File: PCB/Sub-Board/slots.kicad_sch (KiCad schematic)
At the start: 119 parts, among them J10 Address, J11 Type, J12 Address, J13 Type, J14 Address, J15 Type, J16 Address, J17 Type, J18 Power/I2C, J19 GPIO, J2 Power/I2C, J20 Power/I2C, J21 GPIO, J22 Power/I2C, J23 GPIO, J24 Power/I2C, J25 GPIO, J26 Address, J27 Type, J28 Address, J29 Type, J3 GPIO, J30 Address, J31 Type, J32 Address, J33 Type, J4 Power/I2C, J5 GPIO, J6 Power/I2C, J7 GPIO, J8 Power/I2C, J9 GPIO

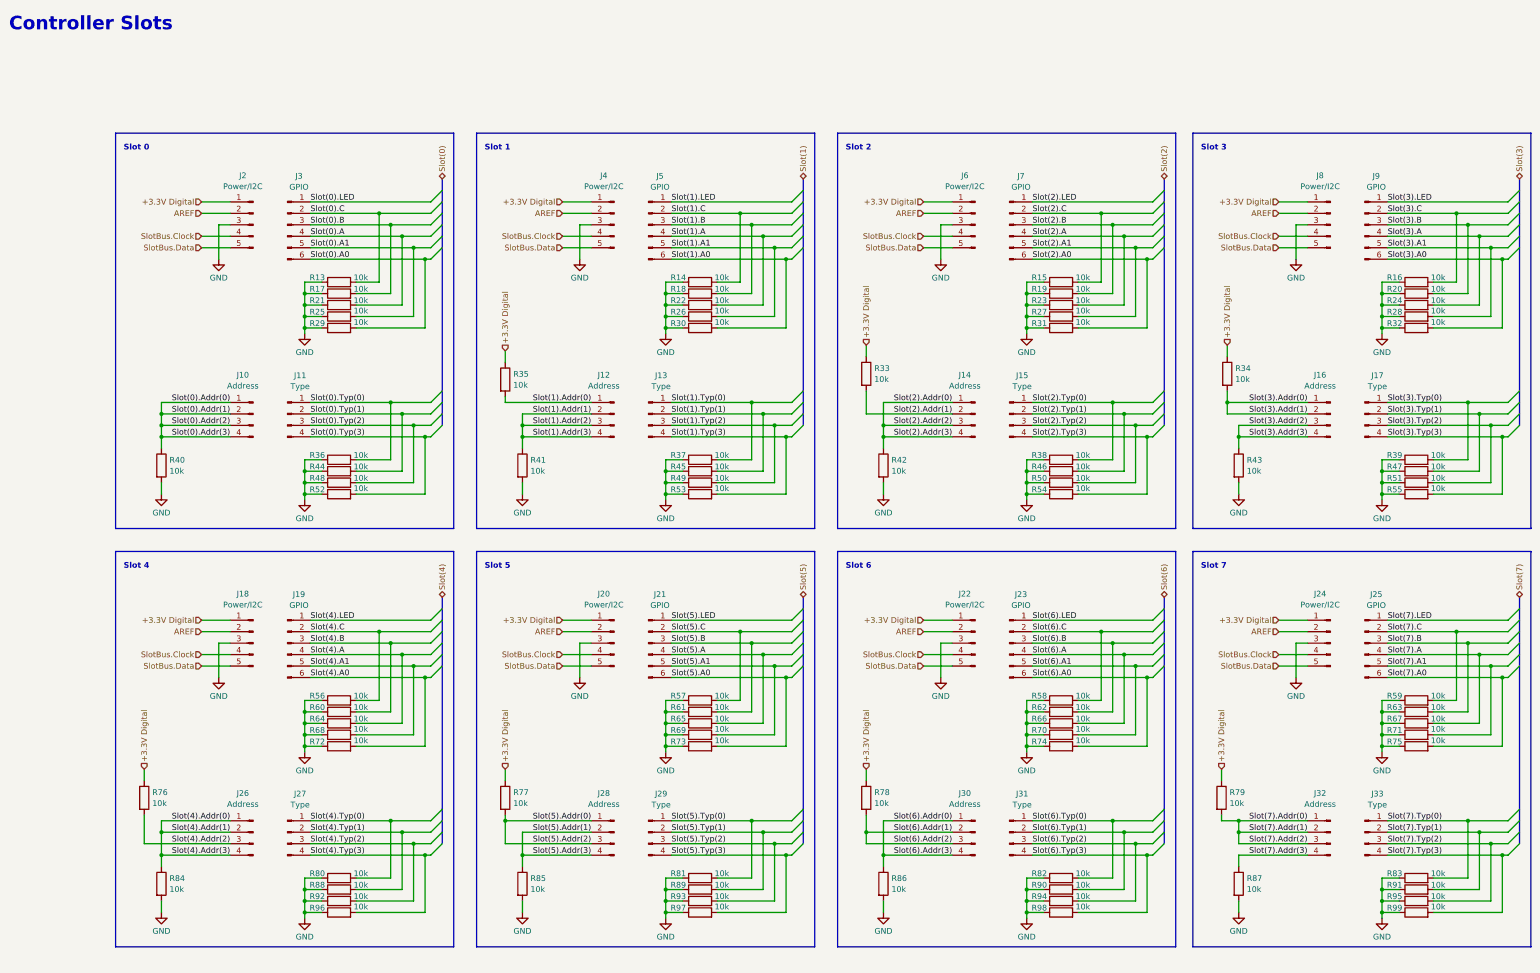
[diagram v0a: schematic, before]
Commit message: Sub-Board PCB before ERC
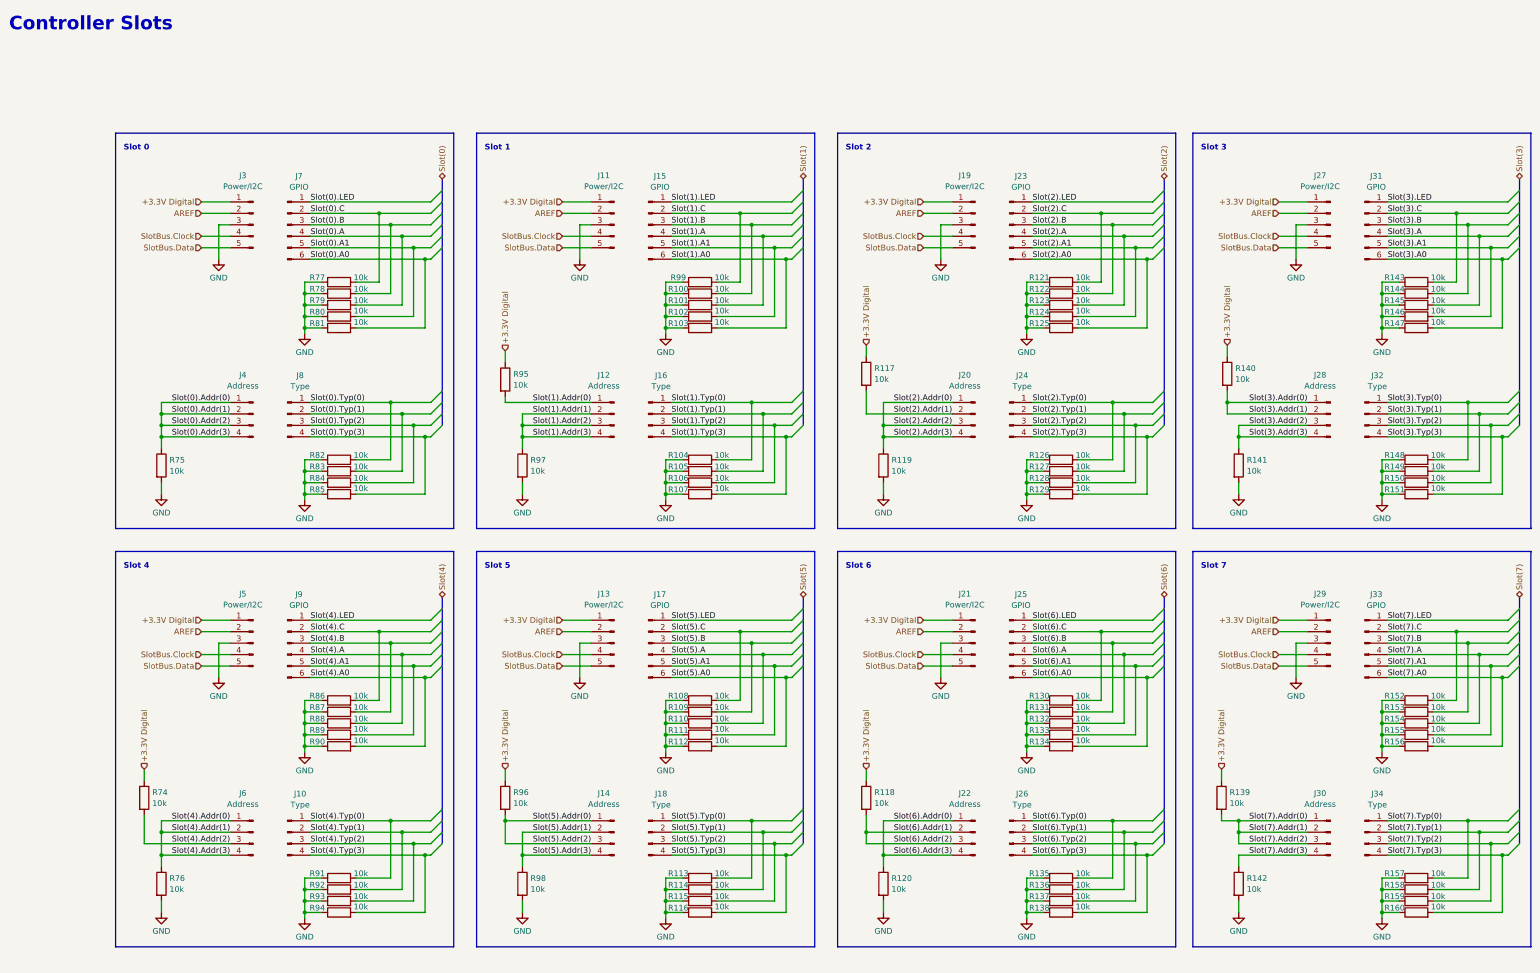
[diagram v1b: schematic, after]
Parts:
- renumbered J27 to J10, J4 to J11, J20 to J13, J28 to J14, J5 to J15, J13 to J16, J21 to J17, J29 to J18, J6 to J19, J14 to J20, J22 to J21, J30 to J22, J7 to J23, J15 to J24, J23 to J25, J31 to J26, J8 to J27, J16 to J28, J24 to J29, J2 to J3, J32 to J30, J9 to J31, J17 to J32, J25 to J33, J33 to J34, J10 to J4, J18 to J5, J26 to J6, J3 to J7, J11 to J8, J19 to J9, R18 to R100, R22 to R101, R26 to R102, R30 to R103, R37 to R104, R45 to R105, R49 to R106, R53 to R107, R57 to R108, R61 to R109, R65 to R110, R69 to R111, R73 to R112, R81 to R113, R89 to R114, R93 to R115, R97 to R116, R33 to R117, R78 to R118, R42 to R119, R86 to R120, R15 to R121, R19 to R122, R23 to R123, R27 to R124, R31 to R125, R38 to R126, R46 to R127, R50 to R128, R54 to R129, R58 to R130, R62 to R131, R66 to R132, R70 to R133, R74 to R134, R82 to R135, R90 to R136, R94 to R137, R98 to R138, R79 to R139, R34 to R140, R43 to R141, R87 to R142, R16 to R143, R20 to R144, R24 to R145, R28 to R146, R32 to R147, R39 to R148, R47 to R149, R51 to R150, R55 to R151, R59 to R152, R63 to R153, R67 to R154, R71 to R155, R75 to R156, R83 to R157, R91 to R158, R95 to R159, R99 to R160, R76 to R74, R40 to R75, R84 to R76, R13 to R77, R17 to R78, R21 to R79, R25 to R80, R29 to R81, R36 to R82, R44 to R83, R48 to R84, R52 to R85, R56 to R86, R60 to R87, R64 to R88, R68 to R89, R72 to R90, R80 to R91, R88 to R92, R92 to R93, R96 to R94, R35 to R95, R77 to R96, R41 to R97, R85 to R98, R14 to R99

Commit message: Sub-Board PCB after ERC
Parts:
- removed R117, R118, R119, R120, R139, R140, R141, R142, R95, R96, R97, R98: 10k, symbol Device:R
- added R100, R101, R102, R103, R104, R105, R106, R107, R126, R127, R128, R129, R130, R131, R132, R133, R152, R153, R154, R155, R156, R157, R158, R159, R77, R78, R79, R80, R81: 10k, symbol Device:R
- renumbered R99 to R108, R100 to R109, R101 to R110, R102 to R111, R103 to R112, R104 to R113, R105 to R114, R106 to R115, R107 to R116, R108 to R117, R109 to R118, R110 to R119, R111 to R120, R112 to R121, R113 to R122, R114 to R123, R115 to R124, R116 to R125, R121 to R134, R122 to R135, R123 to R136, R124 to R137, R125 to R138, R126 to R139, R127 to R140, R128 to R141, R129 to R142, R130 to R143, R131 to R144, R132 to R145, R133 to R146, R134 to R147, R135 to R148, R136 to R149, R137 to R150, R138 to R151, R143 to R160, R144 to R161, R145 to R162, R146 to R163, R147 to R164, R148 to R165, R149 to R166, R150 to R167, R151 to R168, R152 to R169, R153 to R170, R154 to R171, R155 to R172, R156 to R173, R157 to R174, R158 to R175, R159 to R176, R160 to R177, R77 to R82, R78 to R83, R79 to R84, R80 to R85, R81 to R86, R82 to R87, R83 to R88, R84 to R89, R85 to R90, R86 to R91, R87 to R92, R88 to R93, R89 to R94, R90 to R95, R91 to R96, R92 to R97, R93 to R98, R94 to R99
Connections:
- net +3.3V Digital: now also R100.1, R101.1, R102.1, R126.1, R127.1, R128.1, R152.1, R153.1, R154.1, R155.1, R156.1
- net GND: now also R103.2, R104.2, R105.2, R106.2, R107.2, R129.2, R130.2, R131.2, R132.2, R133.2, R157.2, R158.2, R159.2, R77.2, R78.2, R79.2, R80.2, R81.2
- net Slot(0).A renamed Slot0.A
- net Slot(0).A0 renamed Slot0.A0
- net Slot(0).A1 renamed Slot0.A1
- removed net Slot(0).Addr(0): J4.1 (Pin_1), J4.2 (Pin_2), J4.3 (Pin_3), J4.4 (Pin_4), R75.1
- net Slot(0).B renamed Slot0.B
- net Slot(0).C renamed Slot0.C
- net Slot(0).LED renamed Slot0.LED
- net Slot(0).Typ(0) renamed Slot0.Typ0
- net Slot(0).Typ(1) renamed Slot0.Typ1
- net Slot(0).Typ(2) renamed Slot0.Typ2
- net Slot(0).Typ(3) renamed Slot0.Typ3
- net Slot(1).A renamed Slot1.A
- net Slot(1).A0 renamed Slot1.A0
- net Slot(1).A1 renamed Slot1.A1
- net Slot(1).Addr(0) renamed Slot1.Addr0
- net Slot1.Addr0: now also R101.2
- removed net Slot(1).Addr(1): J12.2 (Pin_2), J12.3 (Pin_3), J12.4 (Pin_4)
- net Slot(1).B renamed Slot1.B
- net Slot(1).C renamed Slot1.C
- net Slot(1).LED renamed Slot1.LED
- net Slot(1).Typ(0) renamed Slot1.Typ0
- net Slot(1).Typ(1) renamed Slot1.Typ1
- net Slot(1).Typ(2) renamed Slot1.Typ2
- net Slot(1).Typ(3) renamed Slot1.Typ3
- net Slot(2).A renamed Slot2.A
- net Slot(2).A0 renamed Slot2.A0
- net Slot(2).A1 renamed Slot2.A1
- removed net Slot(2).Addr(0): J20.1 (Pin_1), J20.3 (Pin_3), J20.4 (Pin_4)
- net Slot(2).Addr(1) renamed Slot2.Addr1
- net Slot2.Addr1: now also R127.2
- net Slot(2).B renamed Slot2.B
- net Slot(2).C renamed Slot2.C
- net Slot(2).LED renamed Slot2.LED
- net Slot(2).Typ(0) renamed Slot2.Typ0
- net Slot(2).Typ(1) renamed Slot2.Typ1
- net Slot(2).Typ(2) renamed Slot2.Typ2
- net Slot(2).Typ(3) renamed Slot2.Typ3
- net Slot(3).A renamed Slot3.A
- net Slot(3).A0 renamed Slot3.A0
- net Slot(3).A1 renamed Slot3.A1
- net Slot(3).Addr(0) renamed Slot3.Addr0
- net Slot3.Addr0: now also R155.2; no longer J28.2 (Pin_2)
- net Slot(3).Addr(2) renamed Slot3.Addr2
- net Slot3.Addr2: now also R157.1; no longer J28.4 (Pin_4)
- net Slot(3).B renamed Slot3.B
- net Slot(3).C renamed Slot3.C
- net Slot(3).LED renamed Slot3.LED
- net Slot(3).Typ(0) renamed Slot3.Typ0
- net Slot(3).Typ(1) renamed Slot3.Typ1
- net Slot(3).Typ(2) renamed Slot3.Typ2
- net Slot(3).Typ(3) renamed Slot3.Typ3
- net Slot(4).A renamed Slot4.A
- net Slot(4).A0 renamed Slot4.A0
- net Slot(4).A1 renamed Slot4.A1
- removed net Slot(4).Addr(0): J6.1 (Pin_1), J6.2 (Pin_2), J6.4 (Pin_4), R76.1
- net Slot(4).Addr(2) renamed Slot4.Addr2
- net Slot(4).B renamed Slot4.B
- net Slot(4).C renamed Slot4.C
- net Slot(4).LED renamed Slot4.LED
- net Slot(4).Typ(0) renamed Slot4.Typ0
- net Slot(4).Typ(1) renamed Slot4.Typ1
- net Slot(4).Typ(2) renamed Slot4.Typ2
- net Slot(4).Typ(3) renamed Slot4.Typ3
- net Slot(5).A renamed Slot5.A
- net Slot(5).A0 renamed Slot5.A0
- net Slot(5).A1 renamed Slot5.A1
- net Slot(5).Addr(0) renamed Slot5.Addr0
- net Slot5.Addr0: now also R102.2; no longer J14.3 (Pin_3)
- net Slot(5).Addr(1) renamed Slot5.Addr1
- net Slot5.Addr1: now also R106.1; no longer J14.4 (Pin_4)
- net Slot(5).B renamed Slot5.B
- net Slot(5).C renamed Slot5.C
- net Slot(5).LED renamed Slot5.LED
- net Slot(5).Typ(0) renamed Slot5.Typ0
- net Slot(5).Typ(1) renamed Slot5.Typ1
- net Slot(5).Typ(2) renamed Slot5.Typ2
- net Slot(5).Typ(3) renamed Slot5.Typ3
- net Slot(6).A renamed Slot6.A
- net Slot(6).A0 renamed Slot6.A0
- net Slot(6).A1 renamed Slot6.A1
- net Slot(6).Addr(0) renamed Slot6.Addr0
- net Slot6.Addr0: now also R132.1; no longer J22.4 (Pin_4)
- net Slot(6).Addr(1) renamed Slot6.Addr1
- net Slot6.Addr1: now also R128.2; no longer J22.3 (Pin_3)
- net Slot(6).B renamed Slot6.B
- net Slot(6).C renamed Slot6.C
- net Slot(6).LED renamed Slot6.LED
- net Slot(6).Typ(0) renamed Slot6.Typ0
- net Slot(6).Typ(1) renamed Slot6.Typ1
- net Slot(6).Typ(2) renamed Slot6.Typ2
- net Slot(6).Typ(3) renamed Slot6.Typ3
- net Slot(7).A renamed Slot7.A
- net Slot(7).A0 renamed Slot7.A0
- net Slot(7).A1 renamed Slot7.A1
- removed net Slot(7).Addr(0): J30.1 (Pin_1), J30.2 (Pin_2), J30.3 (Pin_3)
- net Slot(7).Addr(3) renamed Slot7.Addr3
- net Slot7.Addr3: now also R159.1
- net Slot(7).B renamed Slot7.B
- net Slot(7).C renamed Slot7.C
- net Slot(7).LED renamed Slot7.LED
- net Slot(7).Typ(0) renamed Slot7.Typ0
- net Slot(7).Typ(1) renamed Slot7.Typ1
- net Slot(7).Typ(2) renamed Slot7.Typ2
- net Slot(7).Typ(3) renamed Slot7.Typ3
- new net Slot0.Addr0: J4.1 (Pin_1), R75.1
- new net Slot0.Addr1: J4.2 (Pin_2), R76.1
- new net Slot0.Addr2: J4.3 (Pin_3), R77.1
- new net Slot0.Addr3: J4.4 (Pin_4), R78.1
- new net Slot1.Addr1: J12.2 (Pin_2), R103.1
- new net Slot1.Addr2: J12.3 (Pin_3), R104.1
- new net Slot1.Addr3: J12.4 (Pin_4), R105.1
- new net Slot2.Addr0: J20.1 (Pin_1), R129.1
- new net Slot2.Addr2: J20.3 (Pin_3), R130.1
- new net Slot2.Addr3: J20.4 (Pin_4), R131.1
- new net Slot3.Addr1: J28.2 (Pin_2), R153.2
- new net Slot3.Addr3: J28.4 (Pin_4), R158.1
- new net Slot4.Addr0: J6.1 (Pin_1), R79.1
- new net Slot4.Addr1: J6.2 (Pin_2), R80.1
- new net Slot4.Addr3: J6.4 (Pin_4), R81.1
- new net Slot5.Addr2: J14.3 (Pin_3), R100.2
- new net Slot5.Addr3: J14.4 (Pin_4), R107.1
- new net Slot6.Addr2: J22.3 (Pin_3), R126.2
- new net Slot6.Addr3: J22.4 (Pin_4), R133.1
- new net Slot7.Addr0: J30.1 (Pin_1), R156.2
- new net Slot7.Addr1: J30.2 (Pin_2), R154.2
- new net Slot7.Addr2: J30.3 (Pin_3), R152.2
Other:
- moved on the sheet: J10, J13, J14, J17, J18, J21, J22, J25, J26, J29, J30, J33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

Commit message: Sub-Board PCB: Footprint assignments
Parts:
- J10, J12, J14, J16, J18, J20, J22, J24, J26, J28, J30, J32, J34, J4, J6, J8: footprint (none) -> Connector_PinSocket_1.27mm:PinSocket_1x04_P1.27mm_Vertical
- J11, J13, J19, J21, J27, J29, J3, J5: footprint (none) -> Connector_PinSocket_1.27mm:PinSocket_1x05_P1.27mm_Vertical
- J15, J17, J23, J25, J31, J33, J7, J9: footprint (none) -> Connector_PinSocket_1.27mm:PinSocket_1x06_P1.27mm_Vertical
- R100, R101, R102, R103, R104, R105, R106, R107, R108, R109, R110, R111, R112, R113, R114, R115, R116, R117, R118, R119, R120, R121, R122, R123, R124, R125, R126, R127, R128, R129, R130, R131, R132, R133, R134, R135, R136, R137, R138, R139, R140, R141, R142, R143, R144, R145, R146, R147, R148, R149, R150, R151, R152, R153, R154, R155, R156, R157, R158, R159, R160, R161, R162, R163, R164, R165, R166, R167, R168, R169, R170, R171, R172, R173, R174, R175, R176, R177, R74, R75, R76, R77, R78, R79, R80, R81, R82, R83, R84, R85, R86, R87, R88, R89, R90, R91, R92, R93, R94, R95, R96, R97, R98, R99: footprint (none) -> Resistor_SMD:R_0603_1608Metric
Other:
- title: Modular Music Controller – Controller Slots -> Modular Music Controller / Sub-Board / Controller Slots

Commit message: Sub Board PCB: PCB Layout (wip)
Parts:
- J10, J12, J14, J16, J18, J20, J22, J24, J26, J28, J30, J32, J34, J4, J6, J8: footprint Connector_PinSocket_1.27mm:PinSocket_1x04_P1.27mm_Vertical -> Connector_PinHeader_1.27mm:PinHeader_1x04_P1.27mm_Vertical
- J11, J13, J19, J21, J27, J29, J3, J5: footprint Connector_PinSocket_1.27mm:PinSocket_1x05_P1.27mm_Vertical -> Connector_PinHeader_1.27mm:PinHeader_1x05_P1.27mm_Vertical
- J15, J17, J23, J25, J31, J33, J7, J9: footprint Connector_PinSocket_1.27mm:PinSocket_1x06_P1.27mm_Vertical -> Connector_PinHeader_1.27mm:PinHeader_1x06_P1.27mm_Vertical
- R100: renamed from R148; footprint Resistor_SMD:R_0603_1608Metric -> Resistor_SMD:R_0402_1005Metric
- R101: renamed from R149; footprint Resistor_SMD:R_0603_1608Metric -> Resistor_SMD:R_0402_1005Metric
- R102: renamed from R150; footprint Resistor_SMD:R_0603_1608Metric -> Resistor_SMD:R_0402_1005Metric
- R103: renamed from R151; footprint Resistor_SMD:R_0603_1608Metric -> Resistor_SMD:R_0402_1005Metric
- R104: renamed from R152; footprint Resistor_SMD:R_0603_1608Metric -> Resistor_SMD:R_0402_1005Metric
- R105: renamed from R153; footprint Resistor_SMD:R_0603_1608Metric -> Resistor_SMD:R_0402_1005Metric
- R106: renamed from R154; footprint Resistor_SMD:R_0603_1608Metric -> Resistor_SMD:R_0402_1005Metric
- R107: renamed from R155; footprint Resistor_SMD:R_0603_1608Metric -> Resistor_SMD:R_0402_1005Metric
- R108: renamed from R156; footprint Resistor_SMD:R_0603_1608Metric -> Resistor_SMD:R_0402_1005Metric
- R109: renamed from R157; footprint Resistor_SMD:R_0603_1608Metric -> Resistor_SMD:R_0402_1005Metric
- R110: renamed from R158; footprint Resistor_SMD:R_0603_1608Metric -> Resistor_SMD:R_0402_1005Metric
- R111: renamed from R159; footprint Resistor_SMD:R_0603_1608Metric -> Resistor_SMD:R_0402_1005Metric
- R112: renamed from R160; footprint Resistor_SMD:R_0603_1608Metric -> Resistor_SMD:R_0402_1005Metric
- R113: renamed from R161; footprint Resistor_SMD:R_0603_1608Metric -> Resistor_SMD:R_0402_1005Metric
- R114: renamed from R162; footprint Resistor_SMD:R_0603_1608Metric -> Resistor_SMD:R_0402_1005Metric
- R115: renamed from R163; footprint Resistor_SMD:R_0603_1608Metric -> Resistor_SMD:R_0402_1005Metric
- R116: renamed from R164; footprint Resistor_SMD:R_0603_1608Metric -> Resistor_SMD:R_0402_1005Metric
- R117: renamed from R165; footprint Resistor_SMD:R_0603_1608Metric -> Resistor_SMD:R_0402_1005Metric
- R118: renamed from R166; footprint Resistor_SMD:R_0603_1608Metric -> Resistor_SMD:R_0402_1005Metric
- R119: renamed from R167; footprint Resistor_SMD:R_0603_1608Metric -> Resistor_SMD:R_0402_1005Metric
- R120: renamed from R168; footprint Resistor_SMD:R_0603_1608Metric -> Resistor_SMD:R_0402_1005Metric
- R121: renamed from R169; footprint Resistor_SMD:R_0603_1608Metric -> Resistor_SMD:R_0402_1005Metric
- R122: renamed from R170; footprint Resistor_SMD:R_0603_1608Metric -> Resistor_SMD:R_0402_1005Metric
- R123: renamed from R171; footprint Resistor_SMD:R_0603_1608Metric -> Resistor_SMD:R_0402_1005Metric
- R124: renamed from R172; footprint Resistor_SMD:R_0603_1608Metric -> Resistor_SMD:R_0402_1005Metric
- R125: renamed from R173; footprint Resistor_SMD:R_0603_1608Metric -> Resistor_SMD:R_0402_1005Metric
- R126: renamed from R174; footprint Resistor_SMD:R_0603_1608Metric -> Resistor_SMD:R_0402_1005Metric
- R127: renamed from R175; footprint Resistor_SMD:R_0603_1608Metric -> Resistor_SMD:R_0402_1005Metric
- R128: renamed from R176; footprint Resistor_SMD:R_0603_1608Metric -> Resistor_SMD:R_0402_1005Metric
- R129: renamed from R177; footprint Resistor_SMD:R_0603_1608Metric -> Resistor_SMD:R_0402_1005Metric
- R26: renamed from R74; footprint Resistor_SMD:R_0603_1608Metric -> Resistor_SMD:R_0402_1005Metric
- R27: renamed from R75; footprint Resistor_SMD:R_0603_1608Metric -> Resistor_SMD:R_0402_1005Metric
- R28: renamed from R76; footprint Resistor_SMD:R_0603_1608Metric -> Resistor_SMD:R_0402_1005Metric
- R29: renamed from R77; footprint Resistor_SMD:R_0603_1608Metric -> Resistor_SMD:R_0402_1005Metric
- R30: renamed from R78; footprint Resistor_SMD:R_0603_1608Metric -> Resistor_SMD:R_0402_1005Metric
- R31: renamed from R79; footprint Resistor_SMD:R_0603_1608Metric -> Resistor_SMD:R_0402_1005Metric
- R32: renamed from R80; footprint Resistor_SMD:R_0603_1608Metric -> Resistor_SMD:R_0402_1005Metric
- R33: renamed from R81; footprint Resistor_SMD:R_0603_1608Metric -> Resistor_SMD:R_0402_1005Metric
- R34: renamed from R82; footprint Resistor_SMD:R_0603_1608Metric -> Resistor_SMD:R_0402_1005Metric
- R35: renamed from R83; footprint Resistor_SMD:R_0603_1608Metric -> Resistor_SMD:R_0402_1005Metric
- R36: renamed from R84; footprint Resistor_SMD:R_0603_1608Metric -> Resistor_SMD:R_0402_1005Metric
- R37: renamed from R85; footprint Resistor_SMD:R_0603_1608Metric -> Resistor_SMD:R_0402_1005Metric
- R38: renamed from R86; footprint Resistor_SMD:R_0603_1608Metric -> Resistor_SMD:R_0402_1005Metric
- R39: renamed from R87; footprint Resistor_SMD:R_0603_1608Metric -> Resistor_SMD:R_0402_1005Metric
- R40: renamed from R88; footprint Resistor_SMD:R_0603_1608Metric -> Resistor_SMD:R_0402_1005Metric
- R41: renamed from R89; footprint Resistor_SMD:R_0603_1608Metric -> Resistor_SMD:R_0402_1005Metric
- R42: renamed from R90; footprint Resistor_SMD:R_0603_1608Metric -> Resistor_SMD:R_0402_1005Metric
- R43: renamed from R91; footprint Resistor_SMD:R_0603_1608Metric -> Resistor_SMD:R_0402_1005Metric
- R44: renamed from R92; footprint Resistor_SMD:R_0603_1608Metric -> Resistor_SMD:R_0402_1005Metric
- R45: renamed from R93; footprint Resistor_SMD:R_0603_1608Metric -> Resistor_SMD:R_0402_1005Metric
- R46: renamed from R94; footprint Resistor_SMD:R_0603_1608Metric -> Resistor_SMD:R_0402_1005Metric
- R47: renamed from R95; footprint Resistor_SMD:R_0603_1608Metric -> Resistor_SMD:R_0402_1005Metric
- R48: renamed from R96; footprint Resistor_SMD:R_0603_1608Metric -> Resistor_SMD:R_0402_1005Metric
- R49: renamed from R97; footprint Resistor_SMD:R_0603_1608Metric -> Resistor_SMD:R_0402_1005Metric
- R50: renamed from R98; footprint Resistor_SMD:R_0603_1608Metric -> Resistor_SMD:R_0402_1005Metric
- R51: renamed from R99; footprint Resistor_SMD:R_0603_1608Metric -> Resistor_SMD:R_0402_1005Metric
- R52: renamed from R100; footprint Resistor_SMD:R_0603_1608Metric -> Resistor_SMD:R_0402_1005Metric
- R53: renamed from R101; footprint Resistor_SMD:R_0603_1608Metric -> Resistor_SMD:R_0402_1005Metric
- R54: renamed from R102; footprint Resistor_SMD:R_0603_1608Metric -> Resistor_SMD:R_0402_1005Metric
- R55: renamed from R103; footprint Resistor_SMD:R_0603_1608Metric -> Resistor_SMD:R_0402_1005Metric
- R56: renamed from R104; footprint Resistor_SMD:R_0603_1608Metric -> Resistor_SMD:R_0402_1005Metric
- R57: renamed from R105; footprint Resistor_SMD:R_0603_1608Metric -> Resistor_SMD:R_0402_1005Metric
- R58: renamed from R106; footprint Resistor_SMD:R_0603_1608Metric -> Resistor_SMD:R_0402_1005Metric
- R59: renamed from R107; footprint Resistor_SMD:R_0603_1608Metric -> Resistor_SMD:R_0402_1005Metric
- R60: renamed from R108; footprint Resistor_SMD:R_0603_1608Metric -> Resistor_SMD:R_0402_1005Metric
- R61: renamed from R109; footprint Resistor_SMD:R_0603_1608Metric -> Resistor_SMD:R_0402_1005Metric
- R62: renamed from R110; footprint Resistor_SMD:R_0603_1608Metric -> Resistor_SMD:R_0402_1005Metric
- R63: renamed from R111; footprint Resistor_SMD:R_0603_1608Metric -> Resistor_SMD:R_0402_1005Metric
- R64: renamed from R112; footprint Resistor_SMD:R_0603_1608Metric -> Resistor_SMD:R_0402_1005Metric
- R65: renamed from R113; footprint Resistor_SMD:R_0603_1608Metric -> Resistor_SMD:R_0402_1005Metric
- R66: renamed from R114; footprint Resistor_SMD:R_0603_1608Metric -> Resistor_SMD:R_0402_1005Metric
- R67: renamed from R115; footprint Resistor_SMD:R_0603_1608Metric -> Resistor_SMD:R_0402_1005Metric
- R68: renamed from R116; footprint Resistor_SMD:R_0603_1608Metric -> Resistor_SMD:R_0402_1005Metric
- R69: renamed from R117; footprint Resistor_SMD:R_0603_1608Metric -> Resistor_SMD:R_0402_1005Metric
- R70: renamed from R118; footprint Resistor_SMD:R_0603_1608Metric -> Resistor_SMD:R_0402_1005Metric
- R71: renamed from R119; footprint Resistor_SMD:R_0603_1608Metric -> Resistor_SMD:R_0402_1005Metric
- R72: renamed from R120; footprint Resistor_SMD:R_0603_1608Metric -> Resistor_SMD:R_0402_1005Metric
- R73: renamed from R121; footprint Resistor_SMD:R_0603_1608Metric -> Resistor_SMD:R_0402_1005Metric
- R74: renamed from R122; footprint Resistor_SMD:R_0603_1608Metric -> Resistor_SMD:R_0402_1005Metric
- R75: renamed from R123; footprint Resistor_SMD:R_0603_1608Metric -> Resistor_SMD:R_0402_1005Metric
- R76: renamed from R124; footprint Resistor_SMD:R_0603_1608Metric -> Resistor_SMD:R_0402_1005Metric
- R77: renamed from R125; footprint Resistor_SMD:R_0603_1608Metric -> Resistor_SMD:R_0402_1005Metric
- R78: renamed from R126; footprint Resistor_SMD:R_0603_1608Metric -> Resistor_SMD:R_0402_1005Metric
- R79: renamed from R127; footprint Resistor_SMD:R_0603_1608Metric -> Resistor_SMD:R_0402_1005Metric
- R80: renamed from R128; footprint Resistor_SMD:R_0603_1608Metric -> Resistor_SMD:R_0402_1005Metric
- R81: renamed from R129; footprint Resistor_SMD:R_0603_1608Metric -> Resistor_SMD:R_0402_1005Metric
- R82: renamed from R130; footprint Resistor_SMD:R_0603_1608Metric -> Resistor_SMD:R_0402_1005Metric
- R83: renamed from R131; footprint Resistor_SMD:R_0603_1608Metric -> Resistor_SMD:R_0402_1005Metric
- R84: renamed from R132; footprint Resistor_SMD:R_0603_1608Metric -> Resistor_SMD:R_0402_1005Metric
- R85: renamed from R133; footprint Resistor_SMD:R_0603_1608Metric -> Resistor_SMD:R_0402_1005Metric
- R86: renamed from R134; footprint Resistor_SMD:R_0603_1608Metric -> Resistor_SMD:R_0402_1005Metric
- R87: renamed from R135; footprint Resistor_SMD:R_0603_1608Metric -> Resistor_SMD:R_0402_1005Metric
- R88: renamed from R136; footprint Resistor_SMD:R_0603_1608Metric -> Resistor_SMD:R_0402_1005Metric
- R89: renamed from R137; footprint Resistor_SMD:R_0603_1608Metric -> Resistor_SMD:R_0402_1005Metric
- R90: renamed from R138; footprint Resistor_SMD:R_0603_1608Metric -> Resistor_SMD:R_0402_1005Metric
- R91: renamed from R139; footprint Resistor_SMD:R_0603_1608Metric -> Resistor_SMD:R_0402_1005Metric
- R92: renamed from R140; footprint Resistor_SMD:R_0603_1608Metric -> Resistor_SMD:R_0402_1005Metric
- R93: renamed from R141; footprint Resistor_SMD:R_0603_1608Metric -> Resistor_SMD:R_0402_1005Metric
- R94: renamed from R142; footprint Resistor_SMD:R_0603_1608Metric -> Resistor_SMD:R_0402_1005Metric
- R95: renamed from R143; footprint Resistor_SMD:R_0603_1608Metric -> Resistor_SMD:R_0402_1005Metric
- R96: renamed from R144; footprint Resistor_SMD:R_0603_1608Metric -> Resistor_SMD:R_0402_1005Metric
- R97: renamed from R145; footprint Resistor_SMD:R_0603_1608Metric -> Resistor_SMD:R_0402_1005Metric
- R98: renamed from R146; footprint Resistor_SMD:R_0603_1608Metric -> Resistor_SMD:R_0402_1005Metric
- R99: renamed from R147; footprint Resistor_SMD:R_0603_1608Metric -> Resistor_SMD:R_0402_1005Metric
